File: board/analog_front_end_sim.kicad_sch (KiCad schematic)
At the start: 34 parts, among them J1 731000105, U1 OPA354, U2 ADG621, U3 LMH6629, U4 OPA820, U5 DAC5571

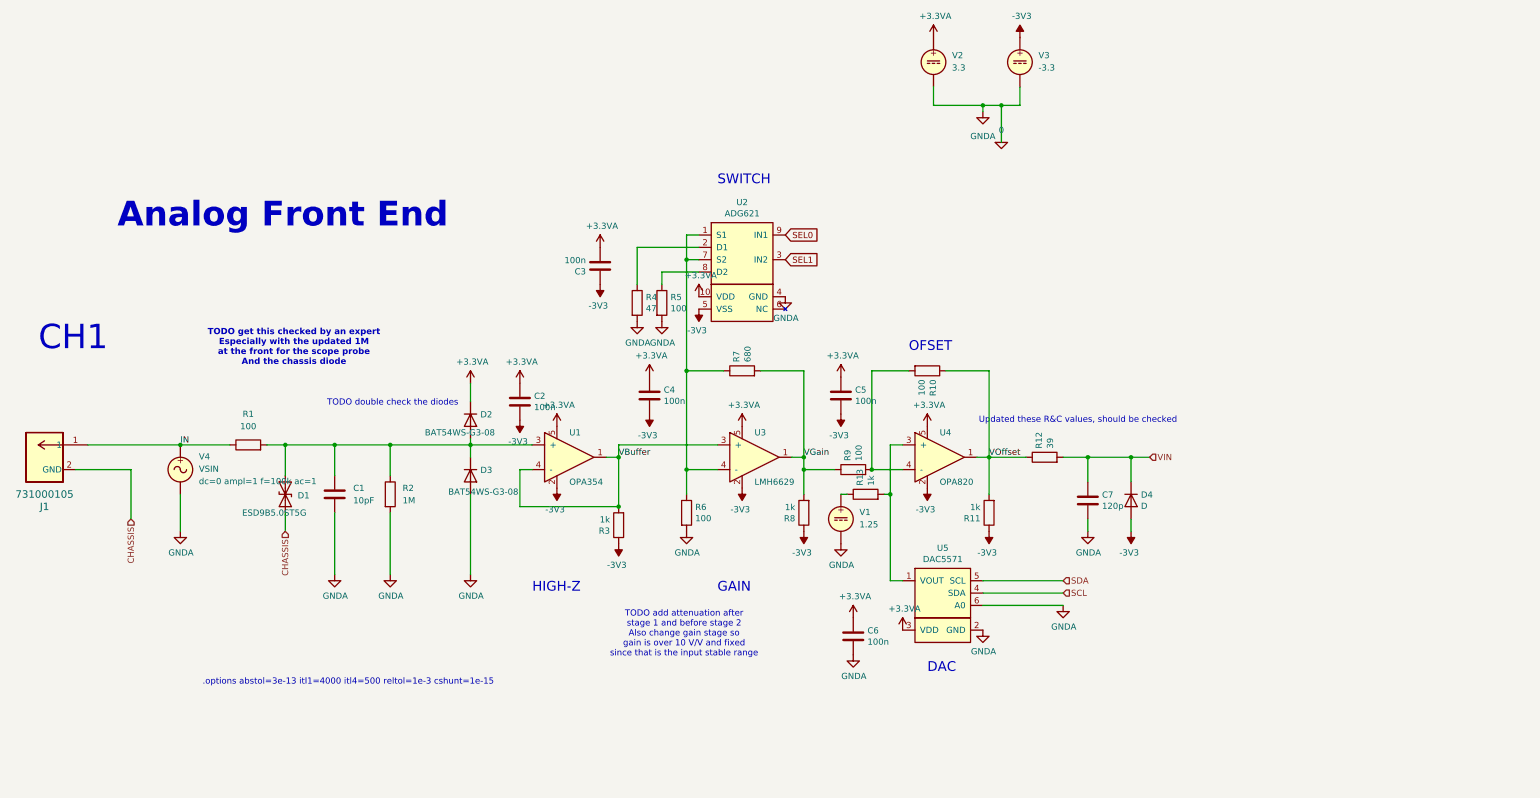
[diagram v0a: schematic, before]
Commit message: Got first version of front end sim working
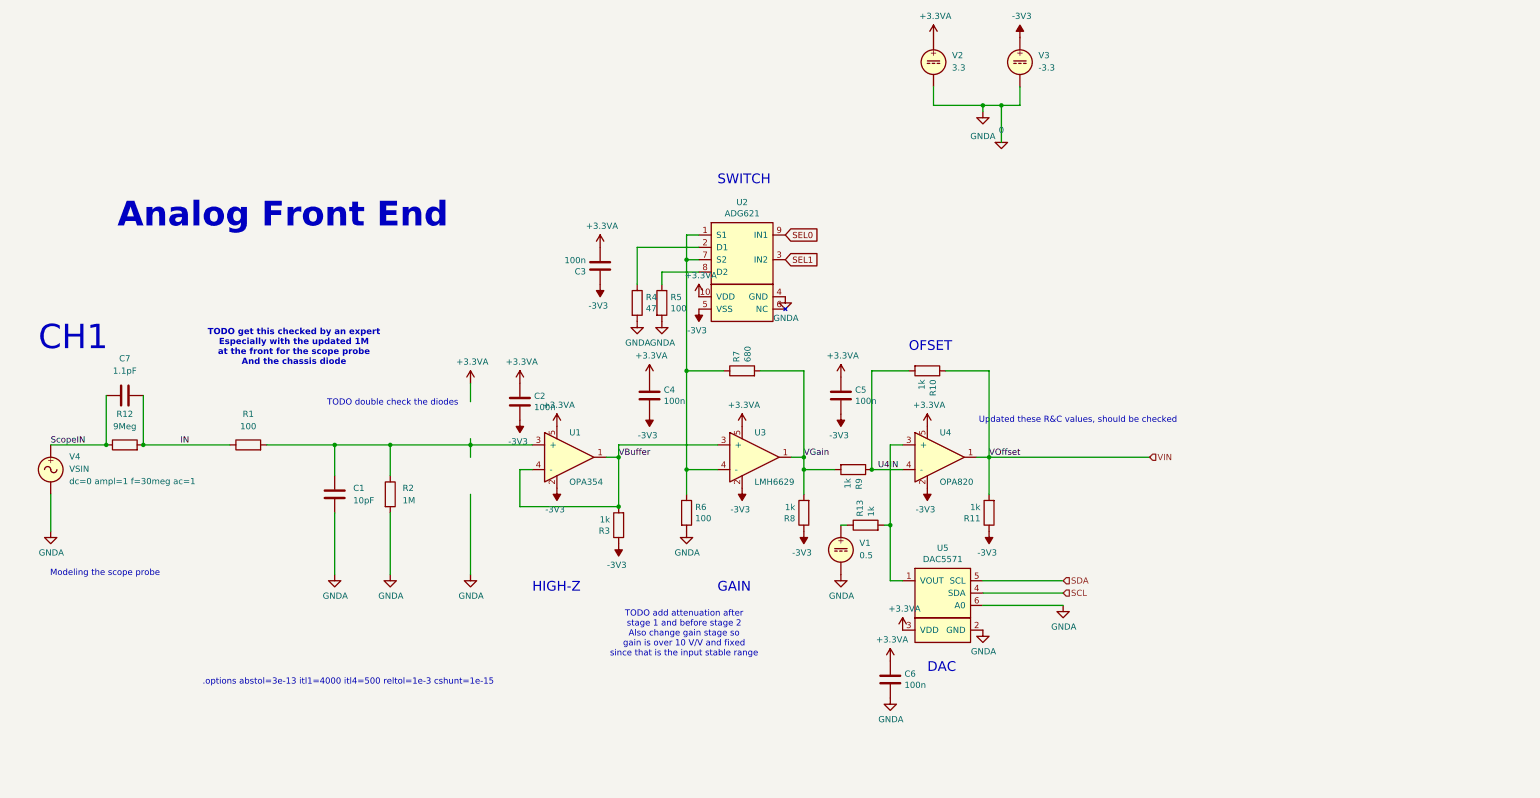
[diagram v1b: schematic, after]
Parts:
- removed D1: ESD9B5.0ST5G, Diode_SMD:D_SOD-923, symbol Diode:ESD9B5.0ST5G
- removed D2, D3: BAT54WS-G3-08, Diode_SMD:D_0603_1608Metric, symbol Device:D
- removed D4: D, Diode_SMD:D_0603_1608Metric, symbol Device:D
- removed J1: 731000105, CONN_73100-0105_MOL, symbol MolexBNC:731000105
- C7: value 120p -> 1.1pF; footprint Capacitor_SMD:C_0603_1608Metric -> (none); MFR. Part # FN18X104K160PSG -> (none)
- R10, R9: value 100 -> 1k; LCSC Part # C22775 -> C21190; MFR. Part # 0603WAF1000T5E -> 0603WAF1001T5E
- R12: value 39 -> 9Meg; footprint Resistor_SMD:R_0603_1608Metric -> (none); MFR. Part # 0603WAF1000T5E -> (none)
- V1: value 1.25 -> 0.5
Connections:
- net 0: no longer C7.2
- net IN: now also C7.2, R12.2; no longer V4.1
- net VGain: now also R9.2; no longer R9.1
- net VIN: now also R10.1, R11.2, U4.1; no longer C7.1, R12.2
- net U4IN: now reaches R10.2, U4.4 (-)
- net U4IN: now also R9.1; no longer R9.2
- removed net VOffset: R10.1, R11.2, R12.1, U4.1
- new net ScopeIN: C7.1, R12.1, V4.1
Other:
- note added: "Modeling the scope probe"
- moved on the sheet: C6, R13, V1, V4

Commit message: More work on front end circuit, and GPIO connections
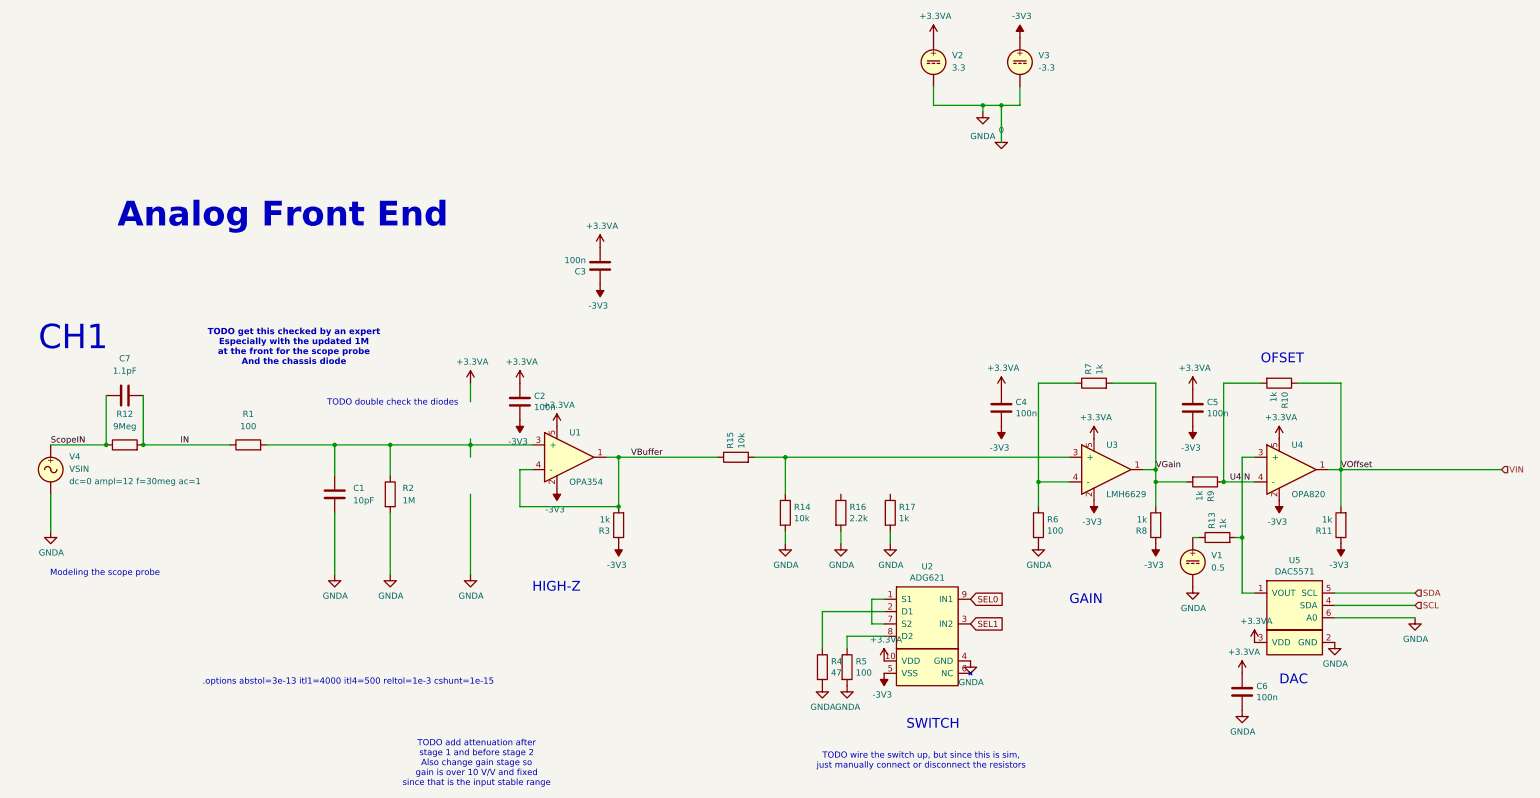
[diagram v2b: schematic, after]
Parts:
- added R14, R15: 10k, Resistor_SMD:R_0603_1608Metric, symbol Device:R
- added R16: 2.2k, Resistor_SMD:R_0603_1608Metric, symbol Device:R
- added R17: 1k, Resistor_SMD:R_0603_1608Metric, symbol Device:R
- R7: value 680 -> 1k; LCSC Part # C23212 -> C21190; MFR. Part # 0603WAF6801T5E -> 0603WAF1001T5E
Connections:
- net 0: now also R14.2, R16.2, R17.2
- net VBuffer: now also R15.1; no longer U3.3 (+)
- net at R6.1, R7.1, U3.4 (-): no longer U2.1 (S1), U2.7 (S2)
- new net: R14.1, R15.2, U3.3 (+)
- new net: U2.1 (S1), U2.7 (S2)
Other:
- note added: "TODO wire the switch up, but since this is sim, just manually connect or disconnect the resistors"
- note removed: "Updated these R&C values, should be checked"
- moved on the sheet: C4, C5, C6, R10, R11, R13, R4, R5, R6, R8, R9, U2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
